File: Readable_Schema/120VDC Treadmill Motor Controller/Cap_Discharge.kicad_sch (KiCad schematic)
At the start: 11 parts, among them J9 OSTT7020150, Q7 DN2450N8-G, Q8 VOM1271T

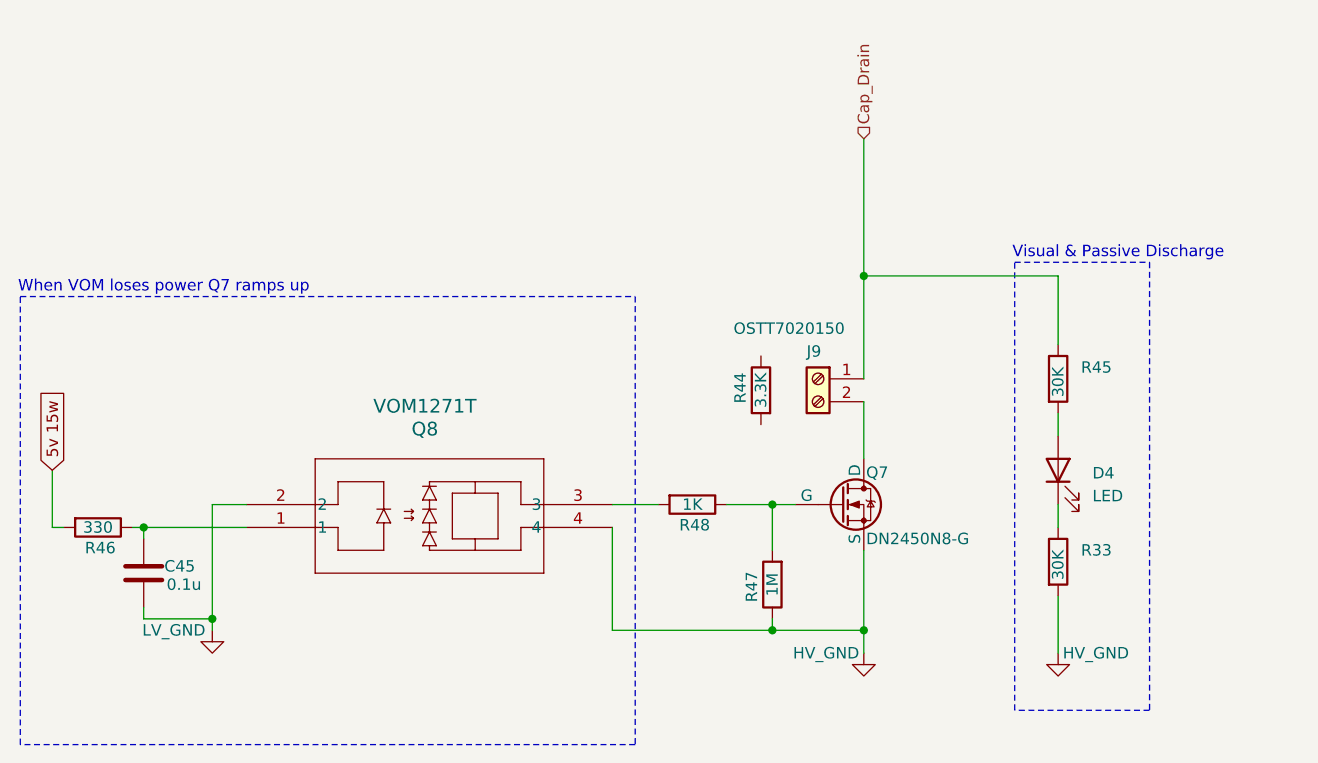
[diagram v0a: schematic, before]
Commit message: -Finished going back and adding some valuable test points. -Realized that 2oz inner copper layer thickness costs way too much so looking at getting 1oz instead. --Need to double check that my pour sizes and inside traces are sized appropiately for 1oz. Not sure how to check
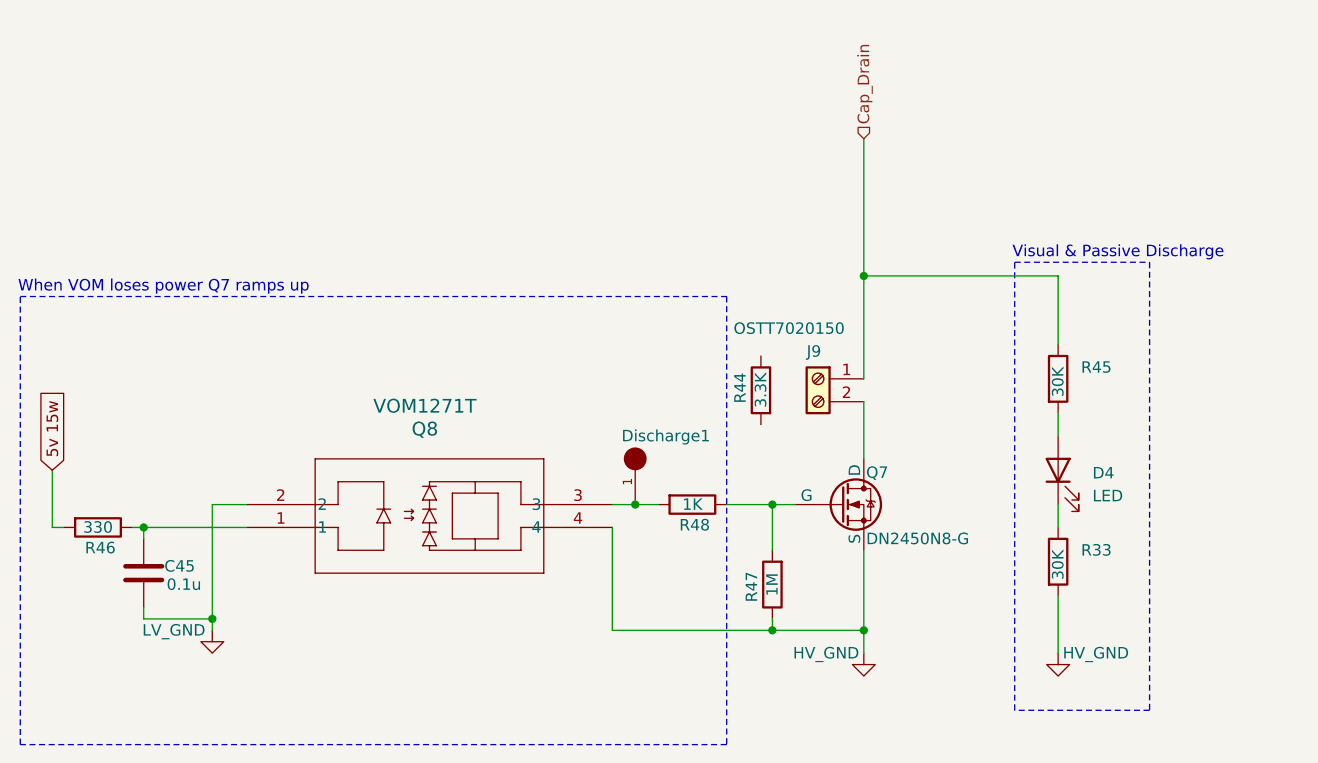
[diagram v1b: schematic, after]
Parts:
- added Discharge1: RCWCTE, Treadmill_Feet:RCWCTE, symbol Treadmill_Comp:RCWCTE
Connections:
- net at Q8.3, R48.2: now also Discharge1.1
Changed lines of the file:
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@@
 	(rectangle
 		(start 32.004 83.566)
-		(end 100.33 133.35)
+		(end 110.49 133.35)
 		(stroke
 			(width 0)
@@
 	)
 	(junction
+		(at 100.33 106.68)
+		(diameter 0)
+		(color 0 0 0 0)
+	)
+	(junction
 		(at 115.57 106.68)
 		(diameter 0)
@@
 	(wire
 		(pts
+			(xy 100.33 106.68) (xy 102.87 106.68)
+		)
+		(stroke
+			(width 0)
+			(type default)
+		)
+	)
+	(wire
+		(pts
 			(xy 35.56 109.22) (xy 36.83 109.22)
 		)
@@
 	(wire
 		(pts
-			(xy 97.79 106.68) (xy 102.87 106.68)
+			(xy 97.79 106.68) (xy 100.33 106.68)
 		)
 		(stroke
@@
 					(unit 1)
 				)
+			)
+		)
+	)
+	(symbol
+		(lib_id "Treadmill_Comp:RCWCTE")
+		(at 100.33 101.6 90)
+		(unit 1)
+		(exclude_from_sim no)
+		(in_bom yes)
+		(on_board yes)
+		(dnp no)
+		(property "Reference" "Discharge1"
+			(at 98.806 99.06 90)
+			(effects
+				(font
+					(size 1.27 1.27)
+				)
+				(justify right)
+			)
+		)
+		(property "Value" "RCWCTE"
+			(at 102.87 102.8699 90)
+			(effects
+				(font
+					(size 1.27 1.27)
+				)
+				(justify right)
+				(hide yes)
+			)
+		)
+		(property "Footprint" "Treadmill_Feet:RCWCTE"
+			(at 100.33 101.6 0)
+			(effects
+				(font
+					(size 1.27 1.27)
+				)
+				(justify bottom)
+				(hide yes)
+			)
+		)
+		(property "Datasheet" "https://www.koaspeer.com/pdfs/RC.pdf"
+			(at 100.33 101.6 0)
+			(effects
+				(font
+					(size 1.27 1.27)
+				)
+				(hide yes)
+			)
+		)
+		(property "Description" "https://www.digikey.com/en/products/detail/koa-speer-electronics-inc/RCWCTE/11476558"
+			(at 100.33 101.6 0)
+			(effects
+				(font
+					(size 1.27 1.27)
+				)
+				(hide yes)
+			)
+		)
+		(property "PARTREV" "1/06/14"
+			(at 100.33 101.6 0)
+			(effects
+				(font
+					(size 1.27 1.27)
+				)
+				(justify bottom)
+				(hide yes)
+			)
+		)
+		(property "SNAPEDA_PN" "RCWCTE"
+			(at 100.33 101.6 0)
+			(effects
+				(font
+					(size 1.27 1.27)
+				)
+				(justify bottom)
+				(hide yes)
+			)
+		)
+		(property "MANUFACTURER" "KOA Speer"
+			(at 100.33 101.6 0)
+			(effects
+				(font
+					(size 1.27 1.27)
+				)
+				(justify bottom)
+				(hide yes)
+			)
+		)
+		(property "MAXIMUM_PACKAGE_HEIGHT" "2 mm"
+			(at 100.33 101.6 0)
+			(effects
+				(font
+					(size 1.27 1.27)
+				)
+				(justify bottom)
+				(hide yes)
+			)
+		)
+		(property "STANDARD" "Manufacturer Recommendations"
+			(at 100.33 101.6 0)
+			(effects
+				(font
+					(size 1.27 1.27)
+				)
+				(justify bottom)
+				(hide yes)
+			)
+		)
+		(pin "1"
+		)
+		(instances
+			(project "120VDC Treadmill Motor Controller"
+				(path "/319bc5c0-2dd5-4df3-a34b-9170833ebccd/1fa0373b-ff98-4bf0-acad-d32450f2dcd0/91d7d3c1-74bb-4c16-a061-6629b37677fd"
+					(reference "Discharge1")
+					(unit 1)
+				)
